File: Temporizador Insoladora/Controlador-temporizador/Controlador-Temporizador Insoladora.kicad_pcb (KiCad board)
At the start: 2 copper layers, 141 x 68.6 mm, 86 parts, among them P1 ICSP, P10 CONN_01X08, P2 VAC12V, P3 CARGA, P4 TRANSF, P5 VAC, P6 OPTO, P7 CONN_02X08, P8 OPTO, P9 OPTO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

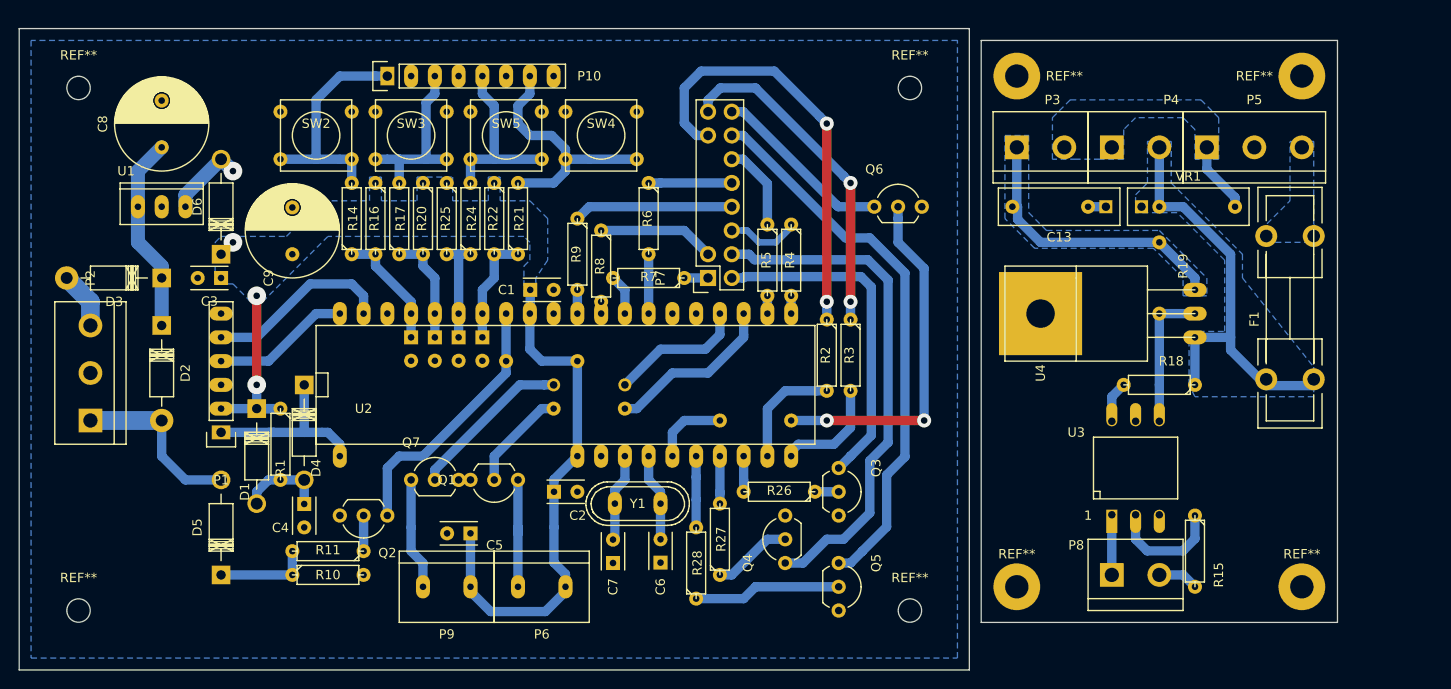
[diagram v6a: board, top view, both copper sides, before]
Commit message: Acomodando las referencias de los compònentes para el top silk
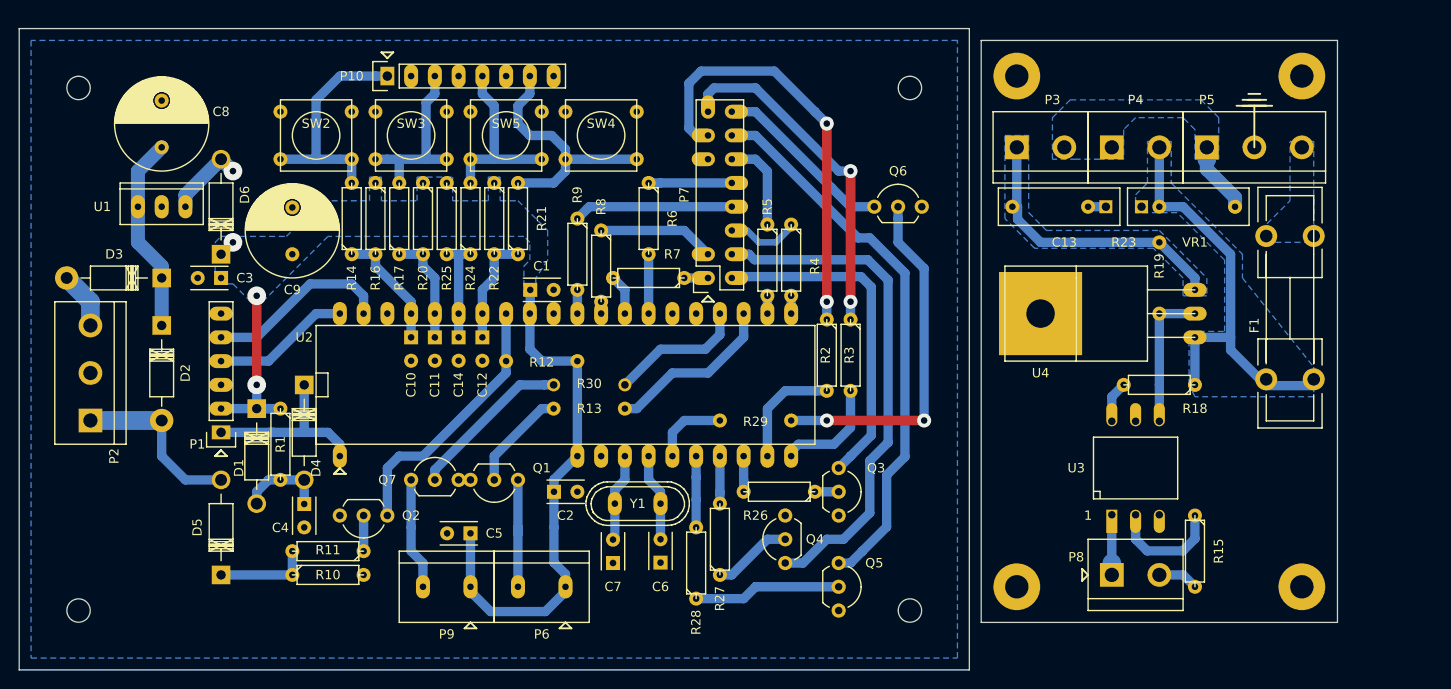
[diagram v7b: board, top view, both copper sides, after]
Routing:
- net Net-(P3-Pad2): track 7.60 -> 12.9 mm
- net /B: track 48.5 -> 50.9 mm
- net /D: track 9.27 -> 10.0 mm
- net Net-(P8-Pad1): track 7.06 -> 6.43 mm

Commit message: Quitando los puentes innecesarios del pcb. Cambio del lugar del diodo de entrada para hacer compatible con el ICSP
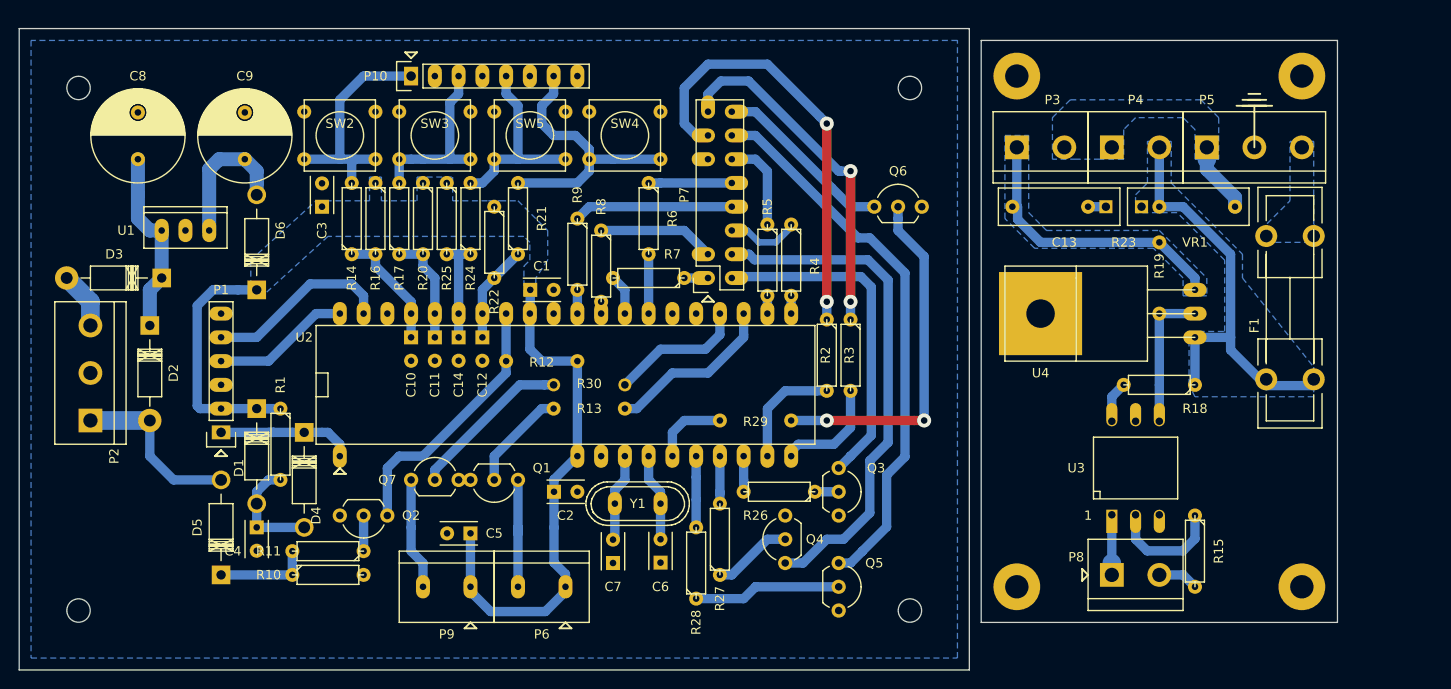
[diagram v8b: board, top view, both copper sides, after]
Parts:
- moved C3 13.2 mm to (97.2, 81.3), turned to 90 degrees
- moved C9 11.4 mm to (88.9, 76.2)
- moved C4 5.66 mm to (90.2, 115.6)
- moved D6 5.39 mm to (90.2, 85.1)
- moved D4 5.08 mm to (95.2, 110.5)
- moved U1 3.59 mm to (82.5, 83.8)
- moved C8 2.84 mm to (77.5, 76.2)
- moved P10 2.54 mm to (106.7, 67.3)
- moved R22 2.54 mm to (115.6, 85.1)
- moved SW2 2.54 mm to (99.1, 73.7)
- moved SW3 2.54 mm to (109.2, 73.7)
- moved SW4 2.54 mm to (129.5, 73.7)
- moved SW5 2.54 mm to (119.4, 73.7)
- moved D2 1.27 mm to (78.7, 99.1)
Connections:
- C9 pad 1: VCC -> Net-(C9-Pad1)
- D6 pad 1: Net-(D6-Pad1) -> Net-(C9-Pad1)
- U1 pad VO: Net-(D6-Pad1) -> Net-(C9-Pad1)
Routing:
- net Net-(C9-Pad1): track 0.00 -> 15.1 mm
- net Net-(D6-Pad1): track 10.3 -> 0.00 mm, vias 1 -> 0
- net VCC: track 79.1 -> 85.6 mm, vias 3 -> 0
- net ~MCLR~/VPP: track 20.1 -> 15.0 mm
- net Net-(P10-Pad7): track 27.4 -> 29.9 mm
- net Net-(C4-Pad1): track 9.42 -> 12.0 mm
- net Net-(P10-Pad5): track 19.6 -> 21.4 mm
- net GPI1: track 12.0 -> 10.5 mm
- net Net-(C8-Pad1): track 21.3 -> 20.1 mm
- net /A: track 45.7 -> 46.7 mm
- net /B: track 50.9 -> 51.6 mm
